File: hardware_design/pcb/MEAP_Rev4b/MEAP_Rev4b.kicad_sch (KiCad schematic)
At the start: 139 parts, among them J1 A_MUX_IN, J10 MUXA, J11 MUXB, J12 MUXC, J13 +3v3 Conn, J14 GND_Conn, J15 SDA, J16 TOUCH_IN, J17 GPIO13, J18 GPIO_18, J19 SCL, J2 GPIO36, J20 CV1, J21 CV2, J22 USB_B_Micro, J23 MIC_IN, J24 LINE_IN, J25 VIN, J26 LINE_OUT, J27 SP_OUT, J28 EM1_COM, J29 EM_X0, J3 MIDI_IN_JACK, J30 EM_X1, J31 EM_X2, J32 EM_X3, J33 EM_X4, J34 EM_X5, J35 EM_X6, J36 EM_X7, J37 R_LINE_OUT, J38 L_LINE_OUT, J39 LINE_IN_JACK, J4 MIDI_OUT_JACK, J40 REG_IN, J5 GPIO15, J6 GPIO16, J7 MIDI_IN, J8 MIDI_OUT, J9 GPIO37, Q1 DMG2301L, SW1 SW_DIP_x01, SW10 BOOT, SW11 SW_SPST, SW2 SW_DIP_x01, SW3 SW_DIP_x01, SW4 SW_DIP_x01, SW5 SW_DIP_x01, SW6 SW_DIP_x01, SW7 SW_DIP_x01, SW8 SW_DIP_x01, SW9 RST, U1 4051, U10 4051, U11 TLV1117-50, U2 PC817, U3 ESP32-S3-WROOM-1, U4 4051, U5 MCP6002-xSN, U7 TLV75733PDRV, U8 SGTL5000XNLA3, U9 PAM8302AAD

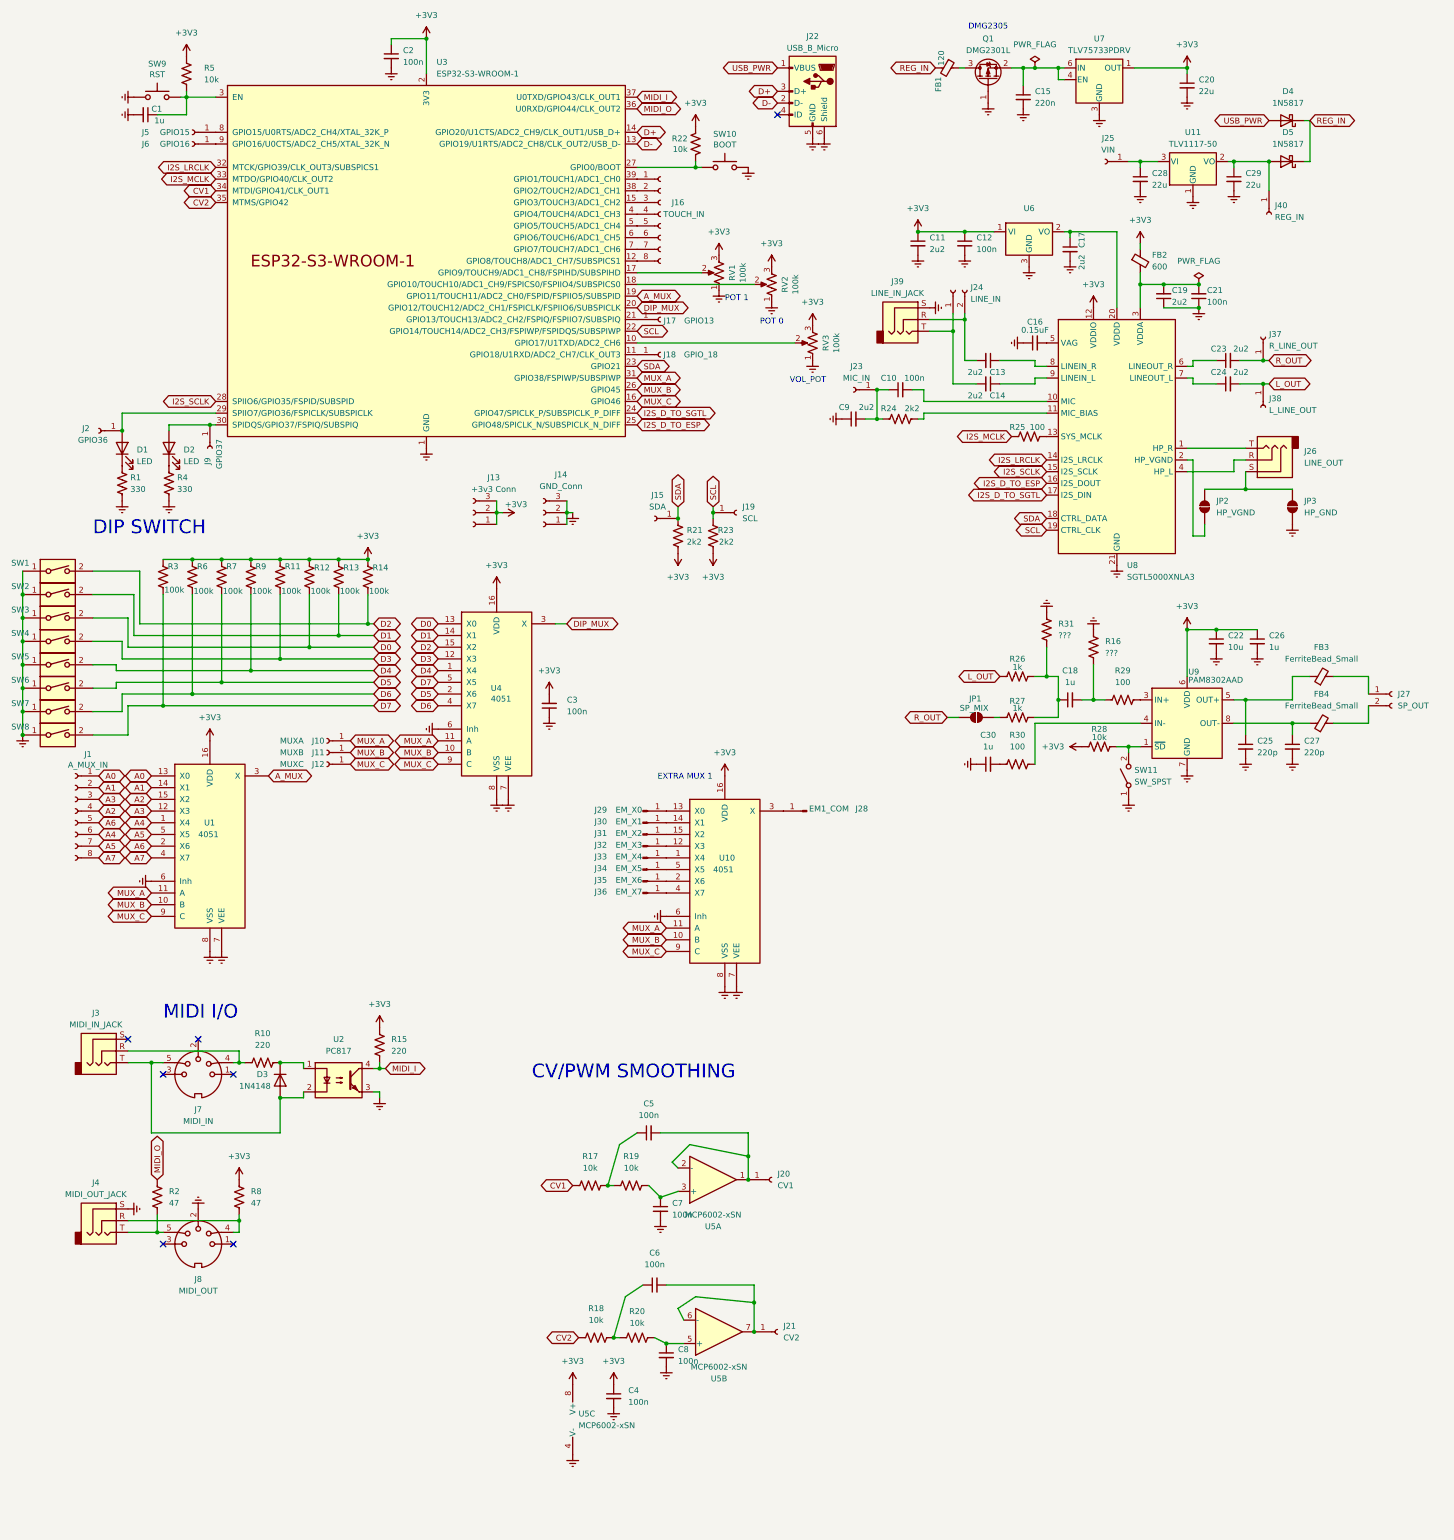
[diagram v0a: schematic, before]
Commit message: new wavetables, code cleanup, more examples and tutorials
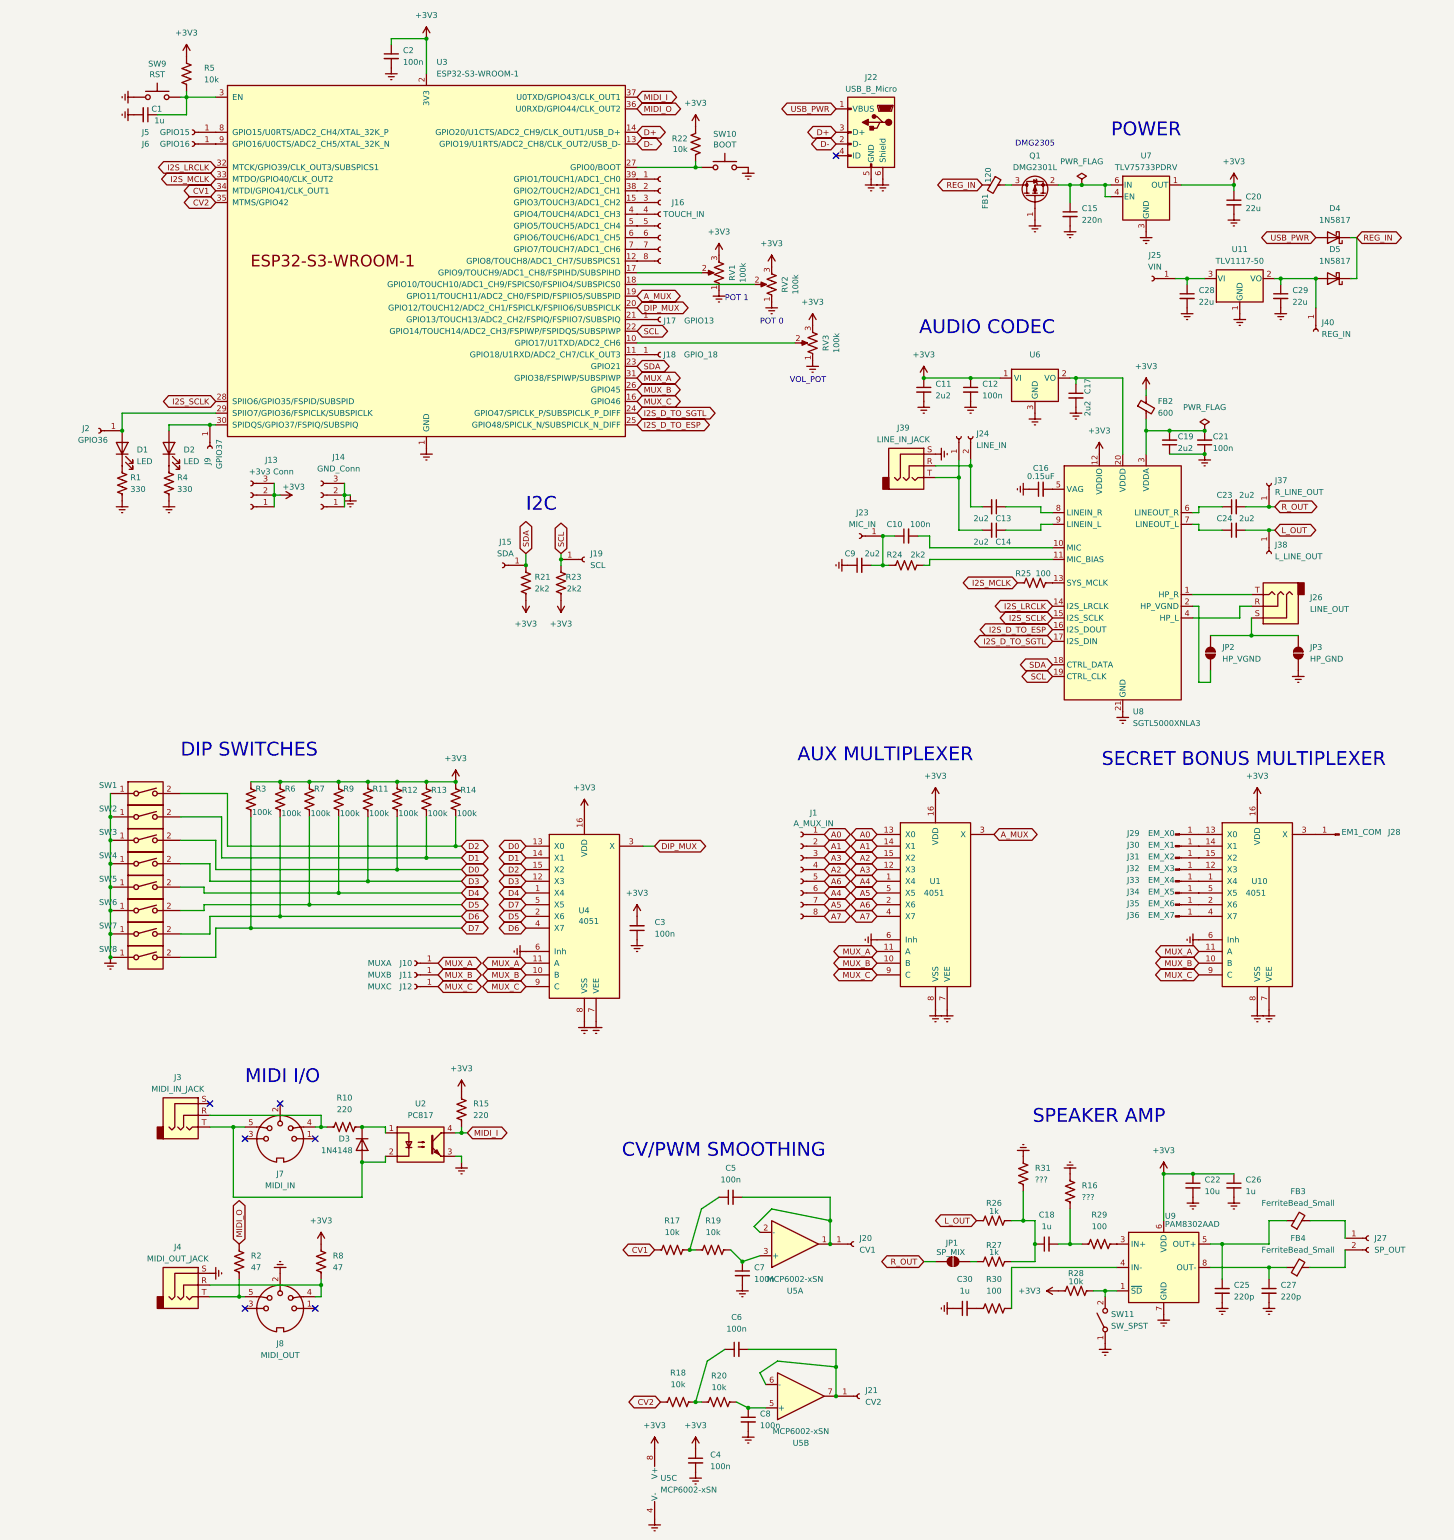
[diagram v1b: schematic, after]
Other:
- note added: "AUDIO CODEC"
- note added: "AUX MULTIPLEXER"
- note added: "DIP SWITCHES"
- note added: "I2C"
- note added: "POWER"
- note added: "SECRET BONUS MULTIPLEXER"
- note added: "SPEAKER AMP"
- note removed: "DIP SWITCH"
- note removed: "EXTRA MUX 1"
- moved on the sheet: C10, C11, C12, C13, C14, C15, C16, C17, C18, C19, C20, C21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
